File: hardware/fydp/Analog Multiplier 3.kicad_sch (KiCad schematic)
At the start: 21 parts, among them J8 Conn_01x02_Pin, U1 LTC2630ISC6-LZ8-TRMPBF, U3 SN74LVC1G3157DCKR, U4 LTC2630ISC6-LZ8-TRMPBF, U5 SN74LVC1G3157DCKR, U6 AD633ARZ-R7

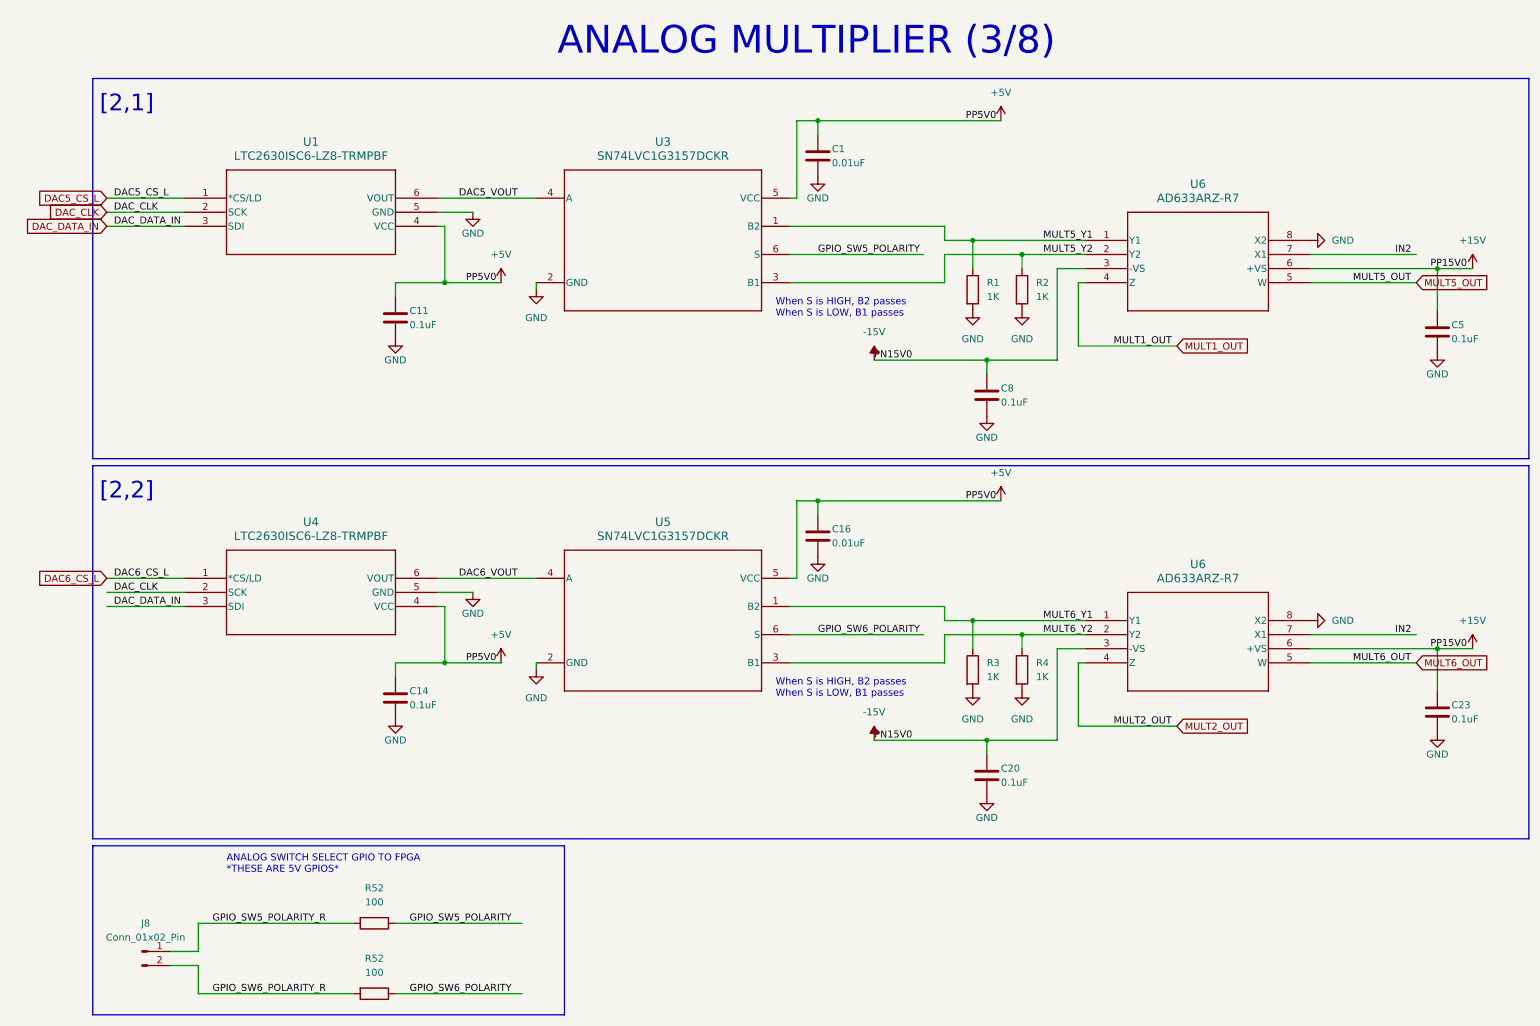
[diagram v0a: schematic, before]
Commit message: Remove 2 channels of multiplier and change ADC
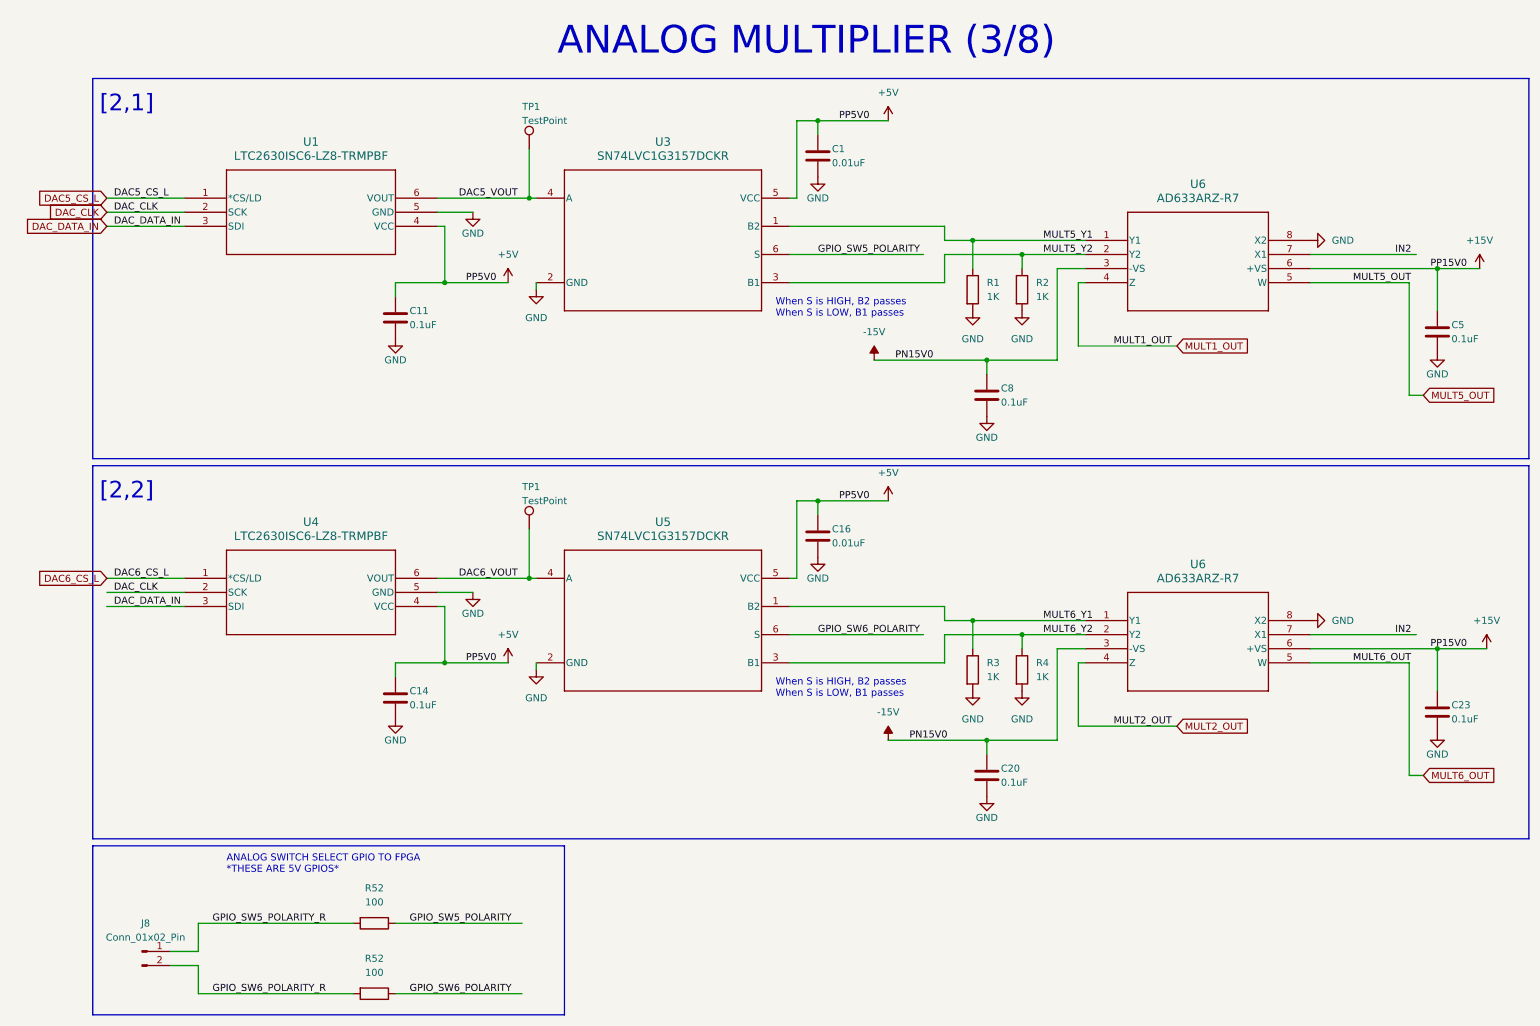
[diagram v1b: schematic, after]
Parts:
- added TP1 (x2): TestPoint, TestPoint:TestPoint_Pad_1.0x1.0mm, symbol Connector:TestPoint
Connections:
- net DAC5_VOUT: now also TP1.1
- net DAC6_VOUT: now also TP1.1

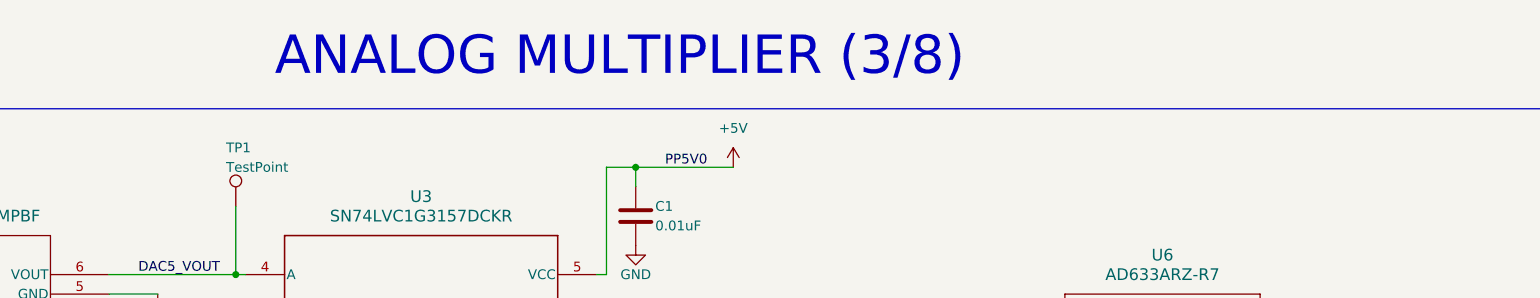
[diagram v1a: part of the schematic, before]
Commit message: Edit schematic titles
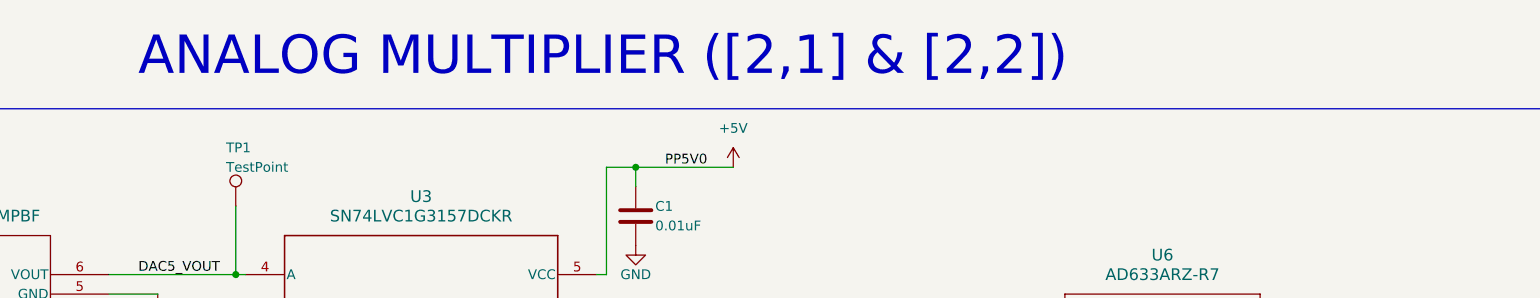
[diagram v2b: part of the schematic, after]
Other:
- note added: "ANALOG MULTIPLIER ([2,1] & [2,2])"
- note removed: "ANALOG MULTIPLIER (3/8)"
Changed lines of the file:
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@@
     (effects (font (size 1.27 1.27)) (justify left bottom))
   )
-  (text "ANALOG MULTIPLIER (3/8)" (at 102.87 22.86 0)
+  (text "ANALOG MULTIPLIER ([2,1] & [2,2])" (at 85.09 22.86 0)
     (effects (font (size 5 5)) (justify left bottom))
   )

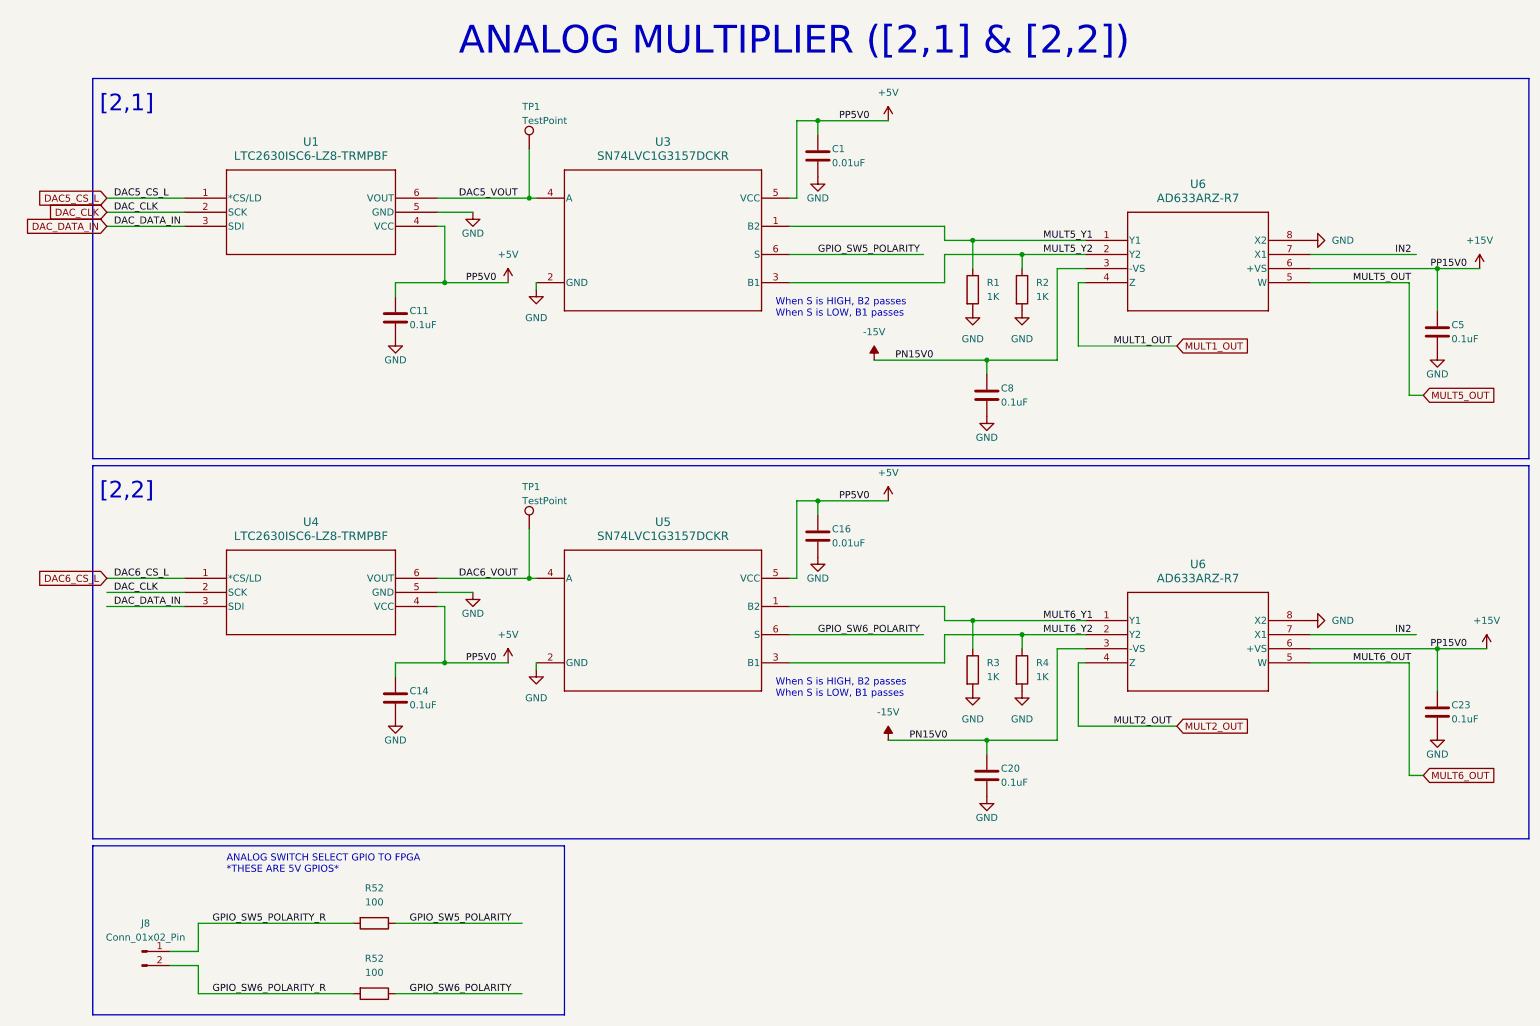
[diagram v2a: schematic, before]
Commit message: Initial layout mostly complete, need to complete lots of routing
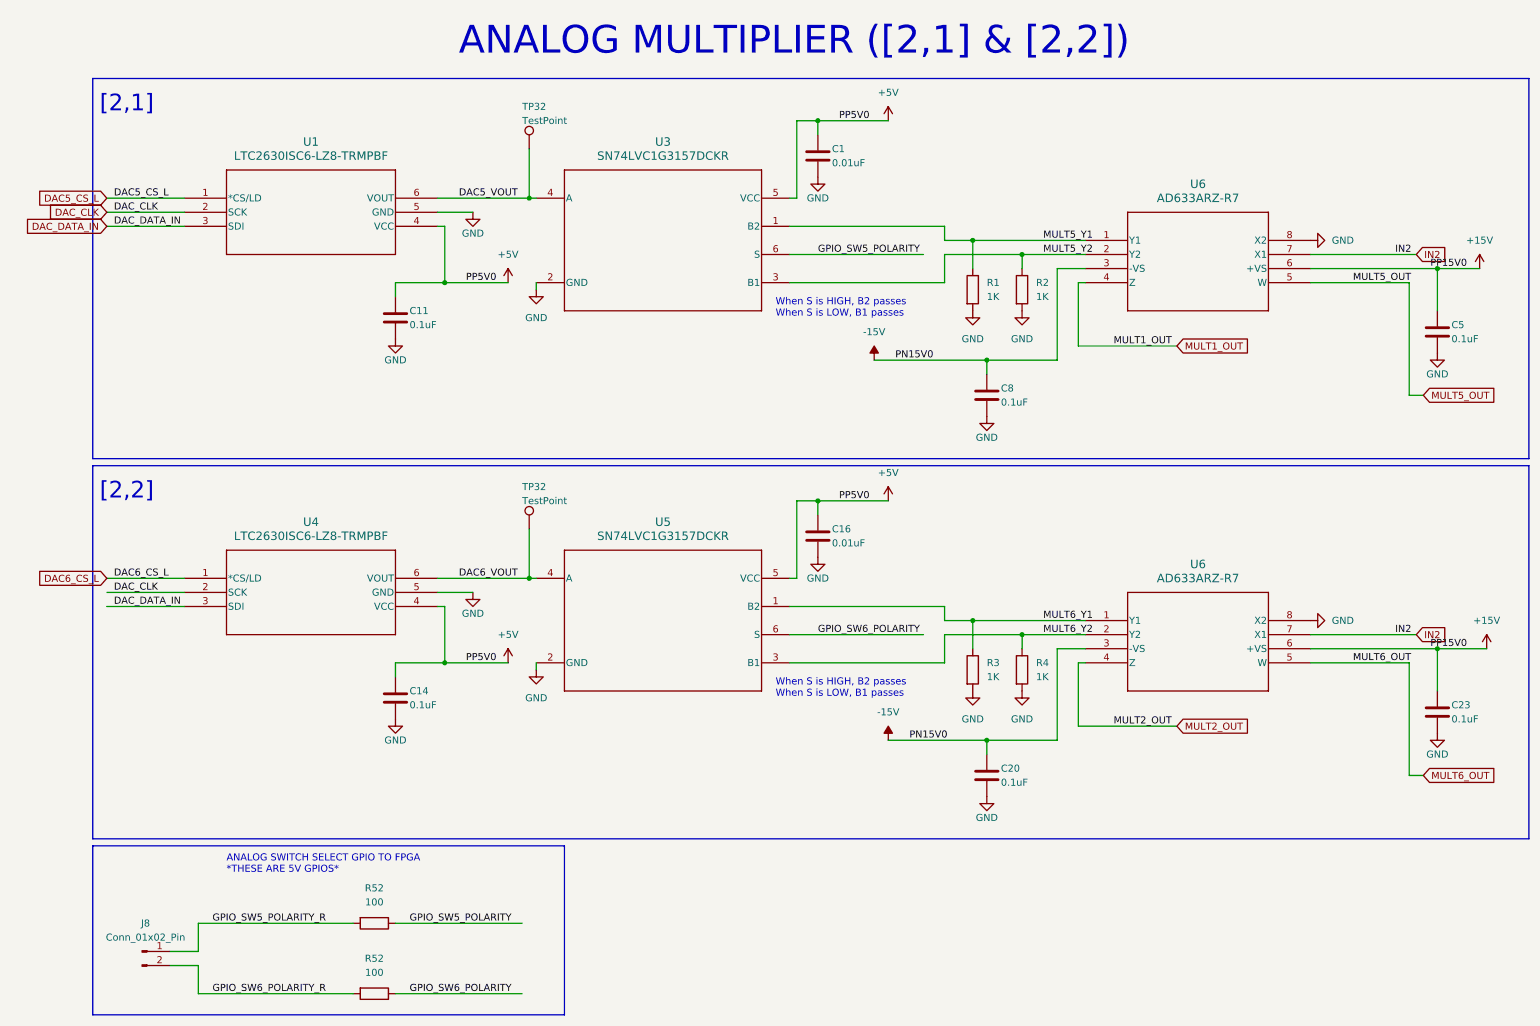
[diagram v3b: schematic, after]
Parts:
- renumbered TP1 to TP32

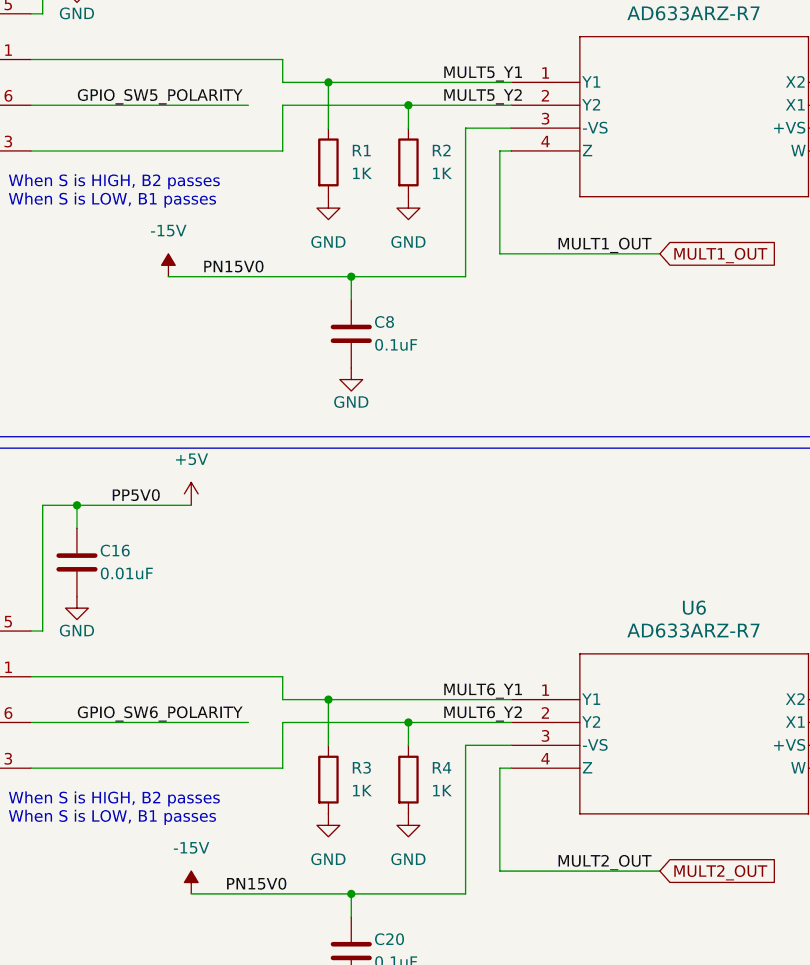
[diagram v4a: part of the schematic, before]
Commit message: Adding JLCPCB BOM notes
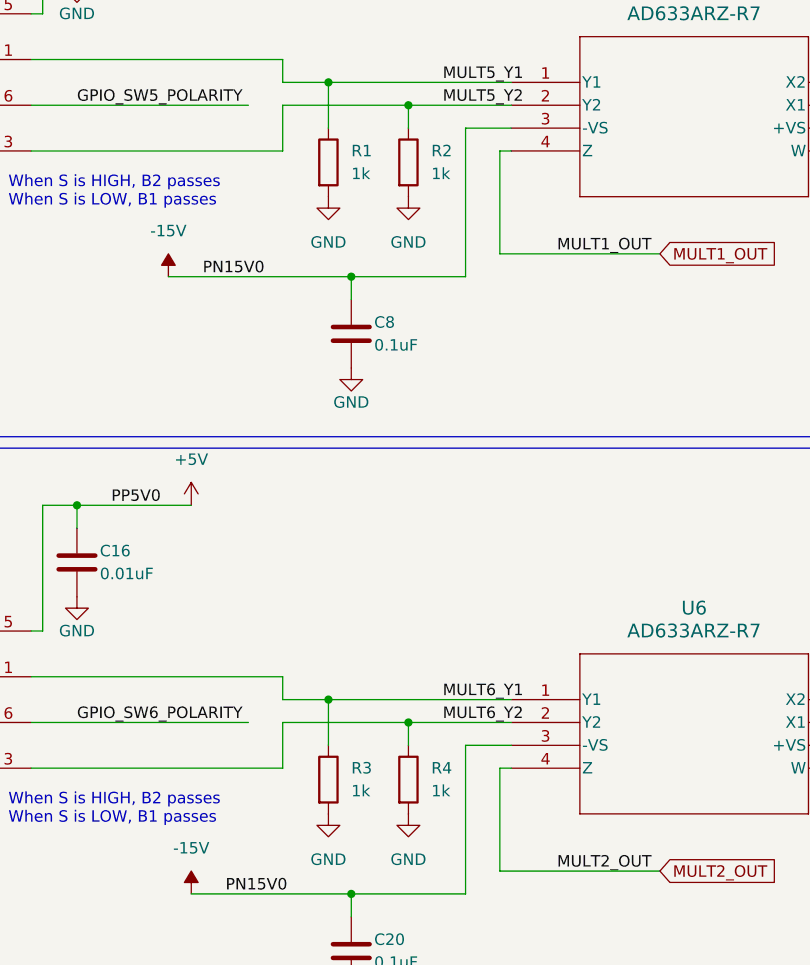
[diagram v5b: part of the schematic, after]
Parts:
- C1, C16: Comment (none) -> 10000 pF ±10% 50V Ceramic Capacitor X7R 0805 (2012 Metric); LCSC (none) -> C83170; MPN (none) -> CC0805KRX7R9BB103
- C11, C14, C20, C23, C5, C8: Comment (none) -> 0.1 µF ±10% 50V Ceramic Capacitor X7R 0805 (2012 Metric); LCSC (none) -> C49678; MPN (none) -> CC0805KRX7R9BB104
- R1, R2, R3, R4: value 1K -> 1k; Comment (none) -> 1 kOhms ±1% 0.125W, 1/8W Chip Resistor 0805 (2012 Metric) M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; LCSC (none) -> C95781; MPN (none) -> RC0805FR-071KL
- R52: Comment (none) -> 100 Ohms ±1% 0.125W, 1/8W Chip Resistor 0805 (2012 Metric) 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; LCSC (none) -> C105577; MPN (none) -> RC0805FR-07100RL
